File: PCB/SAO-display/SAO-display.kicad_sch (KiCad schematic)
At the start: 28 parts, among them CON1 SAO v1.69bis badge, J1 Conn_01x02, J2 Conn_01x02, J3 Conn_01x02, J4 Conn_01x02, J5 Conn_01x02, J6 Conn_01x02

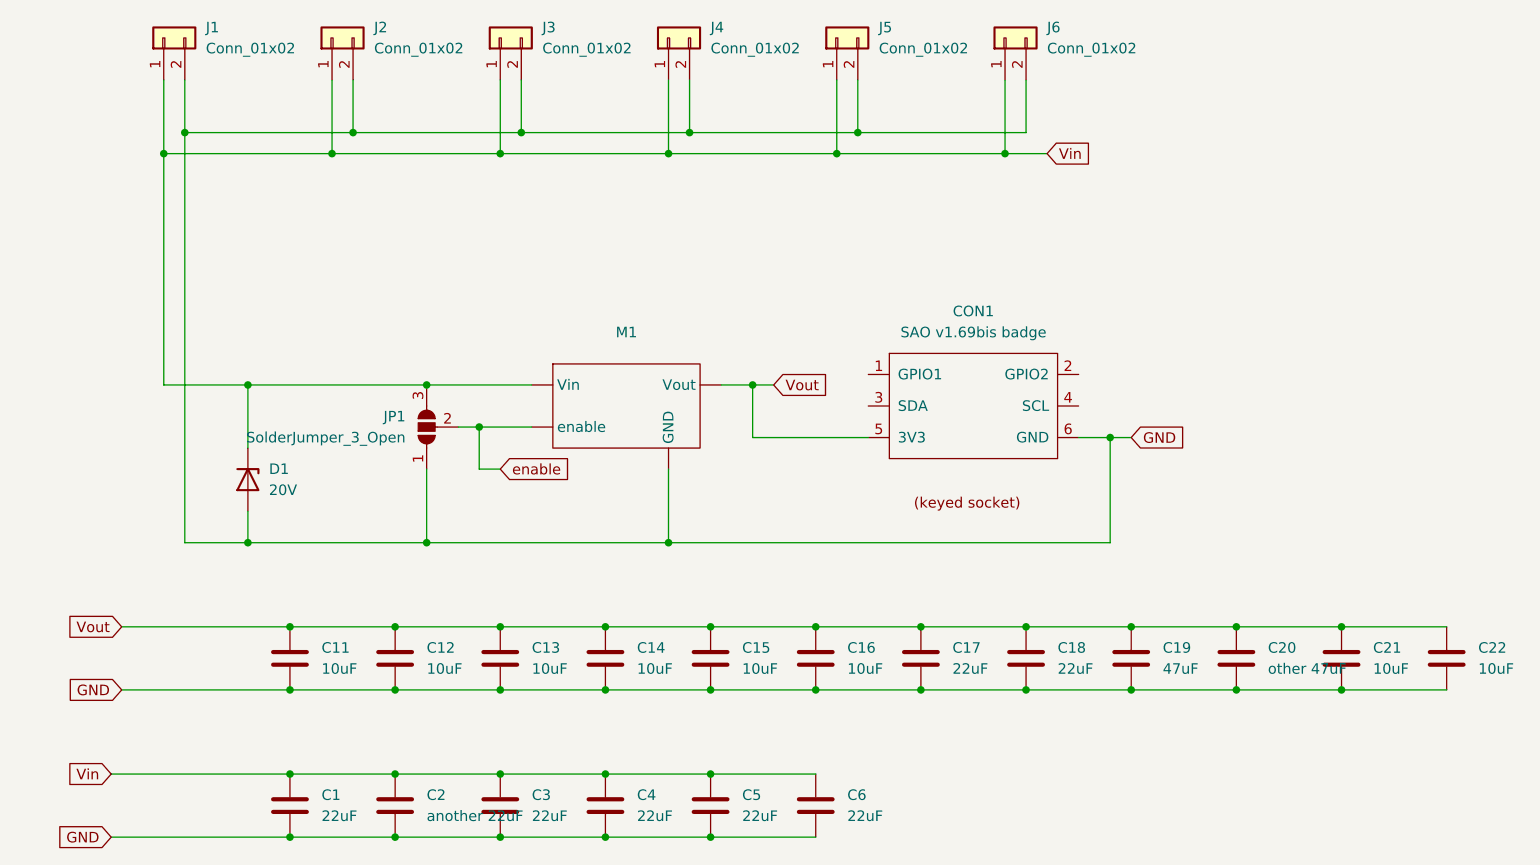
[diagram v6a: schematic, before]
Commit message: flip connections to half the pogo pins; add protection diode
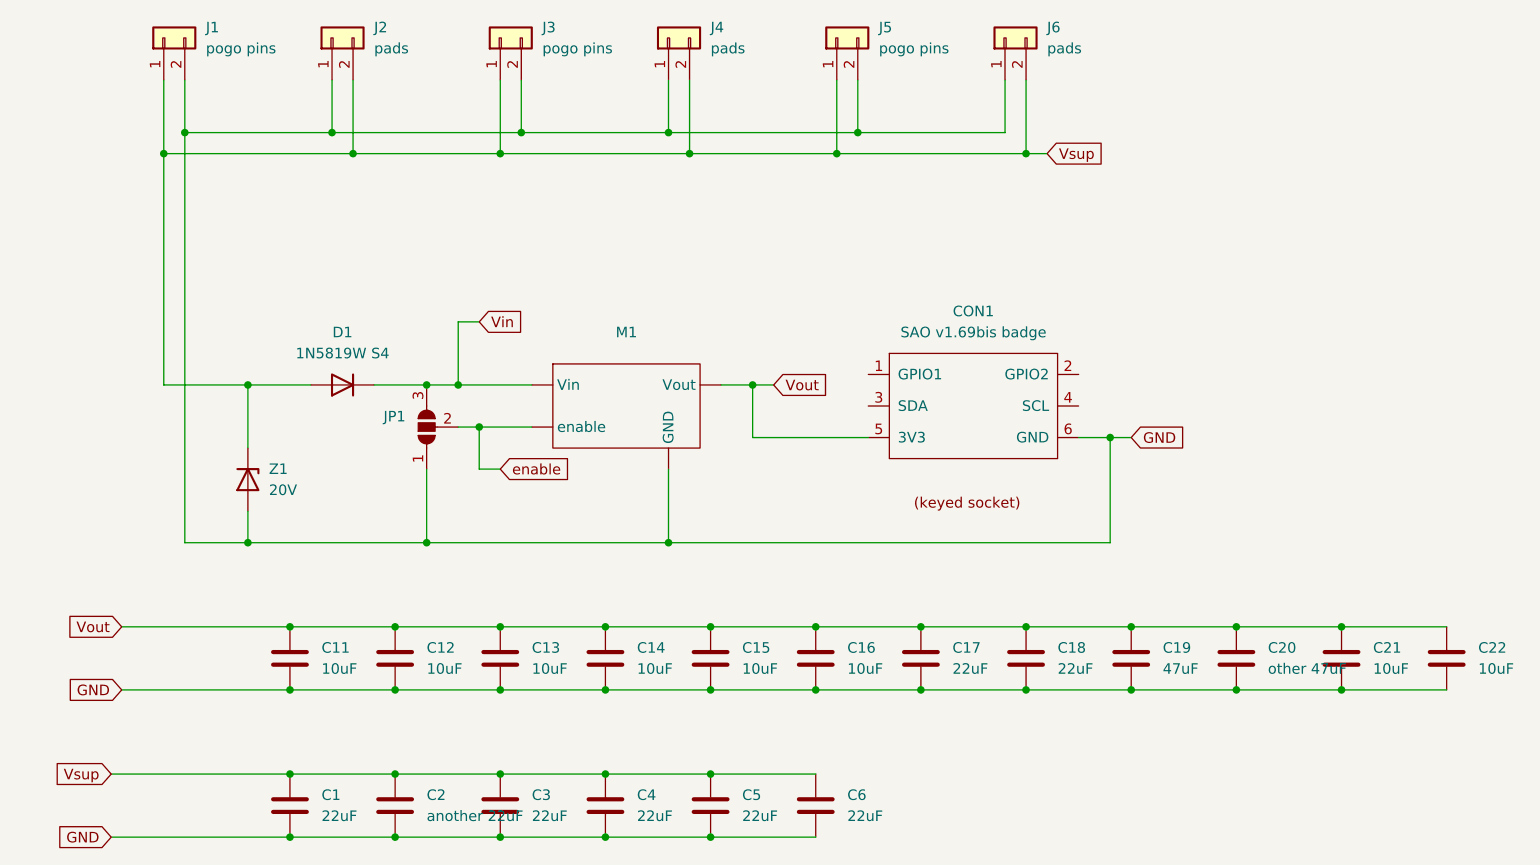
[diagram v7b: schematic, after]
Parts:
- added D1: 1N5819W S4, Diode_SMD:D_SOD-123F, symbol Device:D
- J1, J3, J5: value Conn_01x02 -> pogo pins
- J2, J4, J6: value Conn_01x02 -> pads
- renumbered D1 to Z1
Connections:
- net GND: now also J2.1 (Pin_1), J4.1 (Pin_1), J6.1 (Pin_1); no longer J2.2 (Pin_2), J4.2 (Pin_2), J6.2 (Pin_2)
- net Vin: now also D1.1 (K); no longer C1.1, C2.1, C3.1, C4.1, C5.1, C6.1, J1.1 (Pin_1), J2.1 (Pin_1), J3.1 (Pin_1), J4.1 (Pin_1), J5.1 (Pin_1), J6.1 (Pin_1), Z1.1 (K)
- new net Vsup: C1.1, C2.1, C3.1, C4.1, C5.1, C6.1, D1.2 (A), J1.1 (Pin_1), J2.2 (Pin_2), J3.1 (Pin_1), J4.2 (Pin_2), J5.1 (Pin_1), J6.2 (Pin_2), Z1.1 (K)

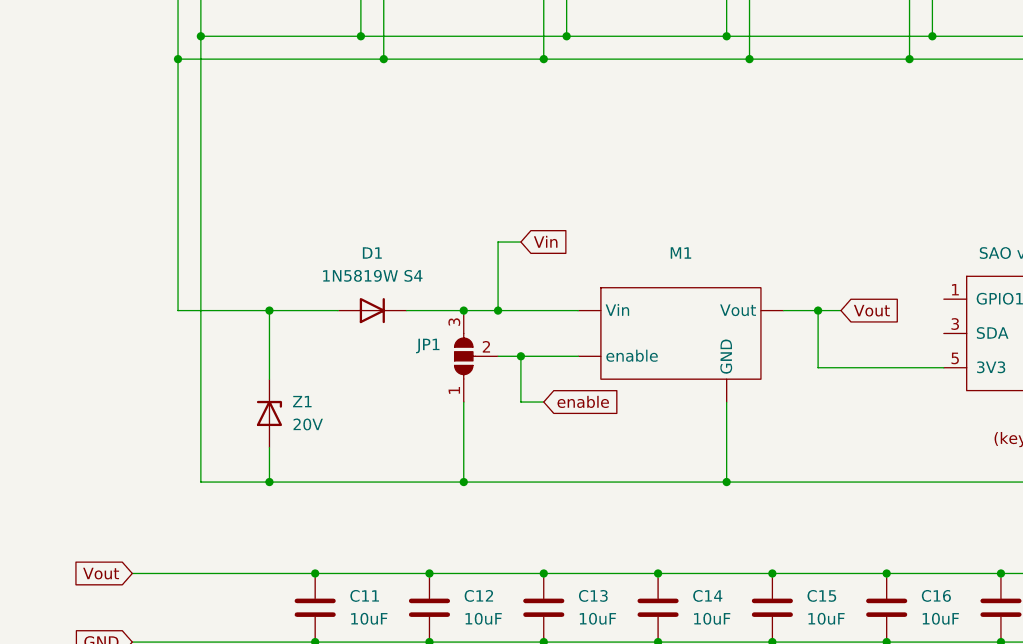
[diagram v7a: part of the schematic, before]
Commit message: add current-limiting resistor to Zener
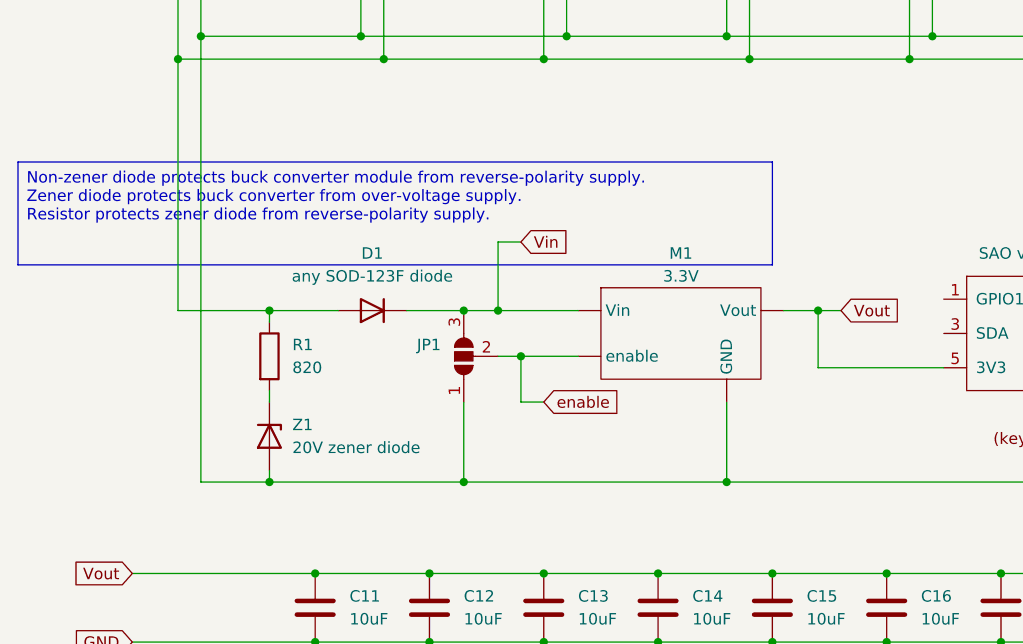
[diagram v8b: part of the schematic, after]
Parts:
- added R1: 820, Resistor_SMD:R_0603_1608Metric_Pad0.98x0.95mm_HandSolder, symbol Device:R
- D1: value 1N5819W S4 -> any SOD-123F diode
- M1: value ~ -> 3.3V
- Z1: value 20V -> 20V zener diode
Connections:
- net Vsup: now also R1.1; no longer Z1.1 (K)
- new net: R1.2, Z1.1 (K)
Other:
- moved on the sheet: Z1
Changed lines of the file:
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@@
 	(generator_version "9.0")
 	(paper "A4")
+	(text_box "Non-zener diode protects buck converter module from reverse-polarity supply.\nZener diode protects buck converter from over-voltage supply.\nResistor protects zener diode from reverse-polarity supply."
+		(exclude_from_sim no)
+		(at 13.97 50.8 0)
+		(size 83.82 11.43)
+		(margins 0.9525 0.9525 0.9525 0.9525)
+		(stroke
+			(width 0)
+			(type solid)
+		)
+		(fill
+			(type none)
+		)
+		(effects
+			(font
+				(size 1.27 1.27)
+			)
+			(justify left top)
+		)
+	)
 	(junction
 		(at 135.89 39.37)
@@
 	)
 	(junction
-		(at 41.91 67.31)
+		(at 46.99 96.52)
 		(diameter 0)
 		(color 0 0 0 0)
 	)
 	(junction
-		(at 46.99 96.52)
+		(at 113.03 39.37)
 		(diameter 0)
 		(color 0 0 0 0)
 	)
 	(junction
-		(at 113.03 39.37)
+		(at 41.91 86.36)
 		(diameter 0)
 		(color 0 0 0 0)
@@
 	)
 	(junction
-		(at 41.91 86.36)
-		(diameter 0)
-		(color 0 0 0 0)
-	)
-	(junction
 		(at 34.29 36.83)
 		(diameter 0)
@@
 	)
 	(junction
+		(at 41.91 67.31)
+		(diameter 0)
+		(color 0 0 0 0)
+	)
+	(junction
 		(at 146.05 73.66)
 		(diameter 0)
@@
 	(wire
 		(pts
+			(xy 41.91 86.36) (xy 63.5 86.36)
+		)
+		(stroke
+			(width 0)
+			(type default)
+		)
+	)
+	(wire
+		(pts
 			(xy 69.85 72.39) (xy 76.2 72.39)
 		)
@@
 	(wire
 		(pts
-			(xy 31.75 39.37) (xy 54.61 39.37)
+			(xy 41.91 67.31) (xy 41.91 68.58)
 		)
 		(stroke
@@
 	(wire
 		(pts
-			(xy 59.69 104.14) (xy 72.39 104.14)
+			(xy 31.75 39.37) (xy 54.61 39.37)
 		)
 		(stroke
@@
 	(wire
 		(pts
-			(xy 92.71 36.83) (xy 115.57 36.83)
+			(xy 59.69 104.14) (xy 72.39 104.14)
 		)
 		(stroke
@@
 	(wire
 		(pts
-			(xy 123.19 96.52) (xy 135.89 96.52)
+			(xy 92.71 36.83) (xy 115.57 36.83)
 		)
 		(stroke
@@
 	(wire
 		(pts
-			(xy 135.89 96.52) (xy 148.59 96.52)
+			(xy 123.19 96.52) (xy 135.89 96.52)
 		)
 		(stroke
@@
 	(wire
 		(pts
-			(xy 46.99 104.14) (xy 59.69 104.14)
+			(xy 135.89 96.52) (xy 148.59 96.52)
 		)
 		(stroke
@@
 	(wire
 		(pts
-			(xy 110.49 104.14) (xy 123.19 104.14)
+			(xy 46.99 104.14) (xy 59.69 104.14)
 		)
 		(stroke
@@
 	(wire
 		(pts
-			(xy 41.91 67.31) (xy 41.91 74.93)
+			(xy 110.49 104.14) (xy 123.19 104.14)
 		)
 		(stroke
@@
 	(wire
 		(pts
-			(xy 59.69 121.92) (xy 72.39 121.92)
+			(xy 41.91 76.2) (xy 41.91 77.47)
 		)
 		(stroke
@@
 	(wire
 		(pts
-			(xy 85.09 114.3) (xy 97.79 114.3)
+			(xy 59.69 121.92) (xy 72.39 121.92)
 		)
 		(stroke
@@
 	(wire
 		(pts
-			(xy 85.09 104.14) (xy 97.79 104.14)
+			(xy 85.09 114.3) (xy 97.79 114.3)
 		)
 		(stroke
@@
 	(wire
 		(pts
-			(xy 146.05 73.66) (xy 146.05 86.36)
+			(xy 85.09 104.14) (xy 97.79 104.14)
 		)
 		(stroke
@@
 	(wire
 		(pts
-			(xy 31.75 30.48) (xy 31.75 39.37)
+			(xy 146.05 73.66) (xy 146.05 86.36)
 		)
 		(stroke
@@
 	(wire
 		(pts
-			(xy 92.71 86.36) (xy 92.71 77.47)
+			(xy 31.75 30.48) (xy 31.75 39.37)
 		)
 		(stroke
@@
 	(wire
 		(pts
-			(xy 34.29 86.36) (xy 41.91 86.36)
+			(xy 92.71 86.36) (xy 92.71 77.47)
 		)
 		(stroke
@@
 	(wire
 		(pts
-			(xy 41.91 82.55) (xy 41.91 86.36)
+			(xy 46.99 121.92) (xy 59.69 121.92)
 		)
 		(stroke
@@
 	(wire
 		(pts
-			(xy 46.99 121.92) (xy 59.69 121.92)
+			(xy 85.09 96.52) (xy 97.79 96.52)
 		)
 		(stroke
@@
 	(wire
 		(pts
-			(xy 85.09 96.52) (xy 97.79 96.52)
+			(xy 97.79 114.3) (xy 110.49 114.3)
 		)
 		(stroke
@@
 	(wire
 		(pts
-			(xy 97.79 114.3) (xy 110.49 114.3)
+			(xy 46.99 96.52) (xy 26.67 96.52)
 		)
 		(stroke
@@
 	(wire
 		(pts
-			(xy 46.99 96.52) (xy 26.67 96.52)
+			(xy 41.91 85.09) (xy 41.91 86.36)
 		)
 		(stroke
@@
 	(wire
 		(pts
-			(xy 41.91 67.31) (xy 49.53 67.31)
+			(xy 148.59 96.52) (xy 161.29 96.52)
 		)
 		(stroke
@@
 	(wire
 		(pts
-			(xy 148.59 96.52) (xy 161.29 96.52)
+			(xy 63.5 86.36) (xy 92.71 86.36)
 		)
 		(stroke
@@
 	(wire
 		(pts
-			(xy 63.5 86.36) (xy 92.71 86.36)
+			(xy 41.91 67.31) (xy 49.53 67.31)
 		)
 		(stroke
@@
 	(wire
 		(pts
-			(xy 41.91 86.36) (xy 63.5 86.36)
+			(xy 34.29 86.36) (xy 41.91 86.36)
 		)
 		(stroke
@@
 	)
 	(symbol
+		(lib_id "Device:R")
+		(at 41.91 72.39 0)
+		(unit 1)
+		(exclude_from_sim no)
+		(in_bom yes)
+		(on_board yes)
+		(dnp no)
+		(fields_autoplaced yes)
+		(property "Reference" "R1"
+			(at 44.45 71.1199 0)
+			(effects
+				(font
+					(size 1.27 1.27)
+				)
+				(justify left)
+			)
+		)
+		(property "Value" "820"
+			(at 44.45 73.6599 0)
+			(effects
+				(font
+					(size 1.27 1.27)
+				)
+				(justify left)
+			)
+		)
+		(property "Footprint" "Resistor_SMD:R_0603_1608Metric_Pad0.98x0.95mm_HandSolder"
+			(at 40.132 72.39 90)
+			(effects
+				(font
+					(size 1.27 1.27)
+				)
+				(hide yes)
+			)
+		)
+		(property "Datasheet" "~"
+			(at 41.91 72.39 0)
+			(effects
+				(font
+					(size 1.27 1.27)
+				)
+				(hide yes)
+			)
+		)
+		(property "Description" "Resistor"
+			(at 41.91 72.39 0)
+			(effects
+				(font
+					(size 1.27 1.27)
+				)
+				(hide yes)
+			)
+		)
+		(pin "2"
+		)
+		(pin "1"
+		)
+		(instances
+			(project ""
+				(path "/d69956fb-1ece-4d71-a86e-9c0e03d8e4b0"
+					(reference "R1")
+					(unit 1)
+				)
+			)
+		)
+	)
+	(symbol
 		(lib_id "Device:C")
 		(at 110.49 100.33 0)
@@
 			)
 		)
-		(property "Value" "1N5819W S4"
+		(property "Value" "any SOD-123F diode"
 			(at 53.34 63.5 0)
 			(effects
@@
 			)
 		)
-		(property "Datasheet" "https://www.lcsc.com/datasheet/lcsc_datasheet_2501131752_TDSEMIC-1N5819W-S4_C42441798.pdf"
+		(property "Datasheet" ""
 			(at 53.34 67.31 0)
 			(effects
@@
 	(symbol
 		(lib_id "Device:D_Zener")
-		(at 41.91 78.74 270)
+		(at 41.91 81.28 270)
 		(unit 1)
 		(exclude_from_sim no)
@@
 		(fields_autoplaced yes)
 		(property "Reference" "Z1"
-			(at 44.45 77.4699 90)
+			(at 44.45 80.0099 90)
 			(effects
 				(font
@@
 			)
 		)
-		(property "Value" "20V"
-			(at 44.45 80.0099 90)
+		(property "Value" "20V zener diode"
+			(at 44.45 82.5499 90)
 			(effects
 				(font
@@
 		)
 		(property "Footprint" "Diode_SMD:D_SOD-123"
-			(at 41.91 78.74 0)
+			(at 41.91 81.28 0)
 			(effects
 				(font
@@
 			)
 		)
-		(property "Datasheet" "https://www.lcsc.com/datasheet/lcsc_datasheet_2410121632_DOWO-BZT52C20_C7544551.pdf"
-			(at 41.91 78.74 0)
+		(property "Datasheet" ""
+			(at 41.91 81.28 0)
 			(effects
 				(font
@@
 		)
 		(property "Description" "Zener diode"
-			(at 41.91 78.74 0)
+			(at 41.91 81.28 0)
 			(effects
 				(font
@@
 		)
 		(property "LCSC Part #" "C7544551"
-			(at 41.91 78.74 90)
+			(at 41.91 81.28 90)
 			(effects
 				(font
@@
 			)
 		)
-		(property "Value" "~"
+		(property "Value" "3.3V"
 			(at 87.63 63.5 0)
 			(effects
